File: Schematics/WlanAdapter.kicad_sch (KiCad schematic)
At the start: 28 parts, among them J1 Barrel_Jack, J2 Conn_02x05_Odd_Even, Q1 AO3400A, U3 ESP32-C3_SUPERMINI

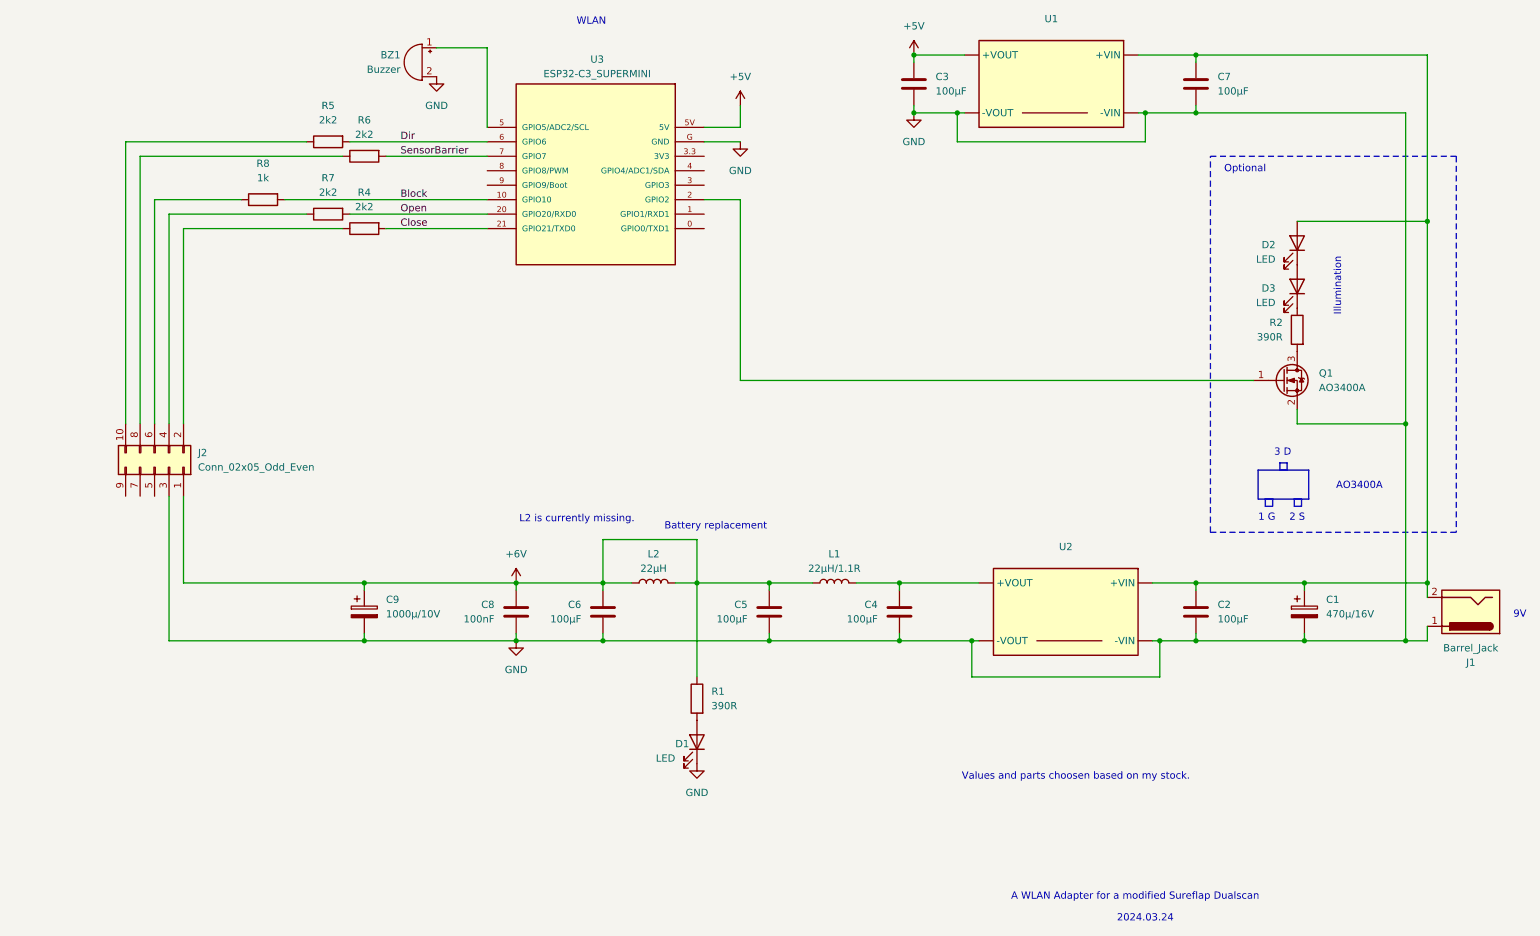
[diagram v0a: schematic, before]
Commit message: Finalize schematics, EspHome works.
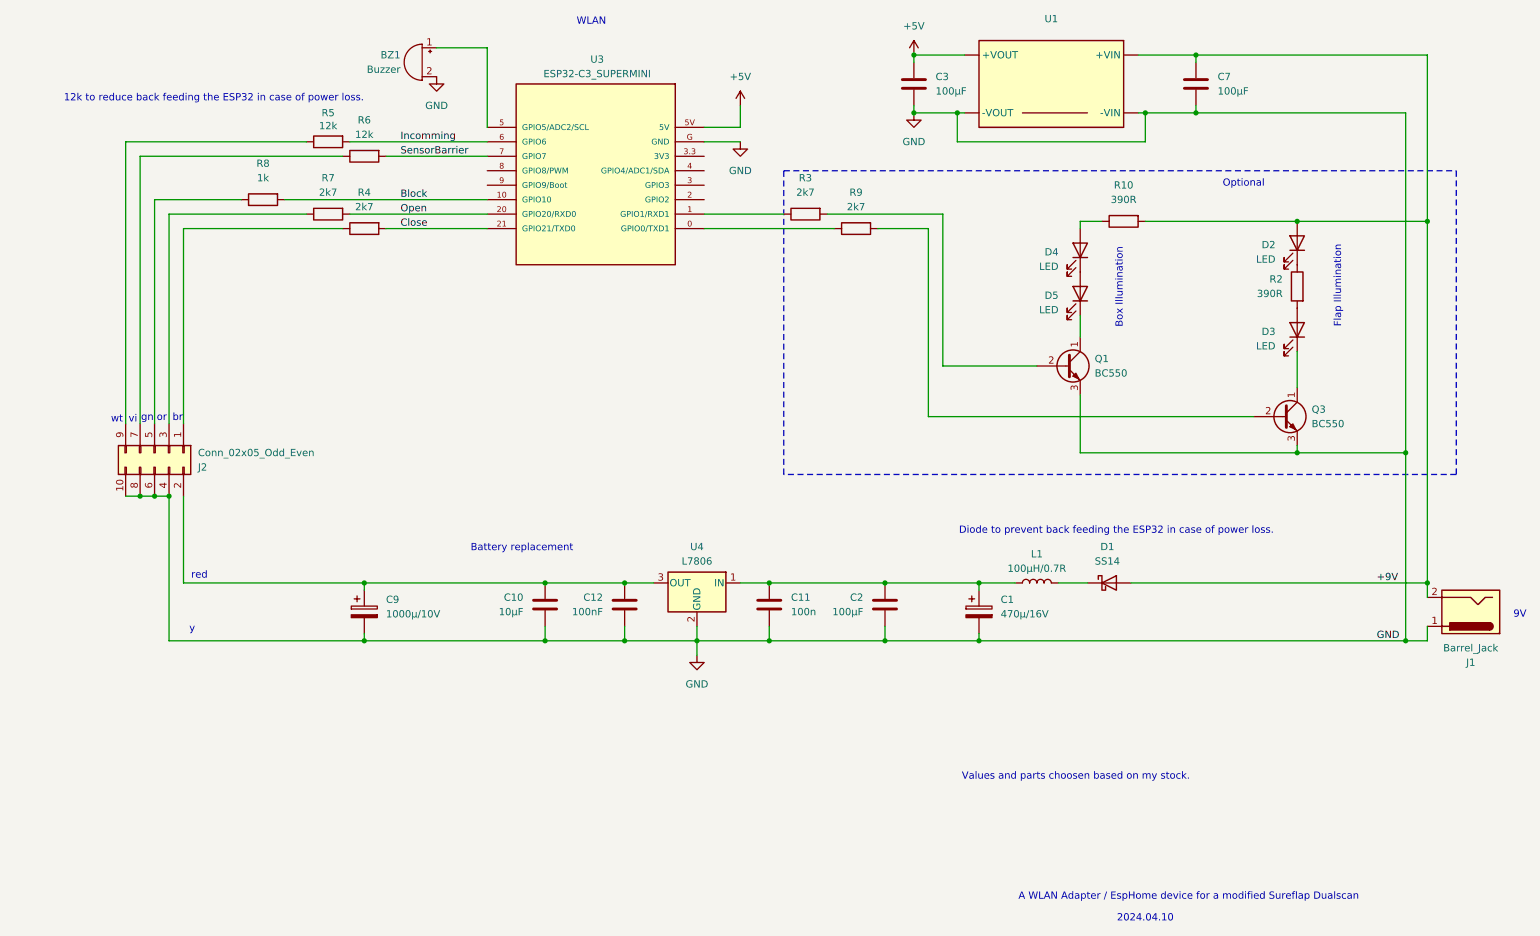
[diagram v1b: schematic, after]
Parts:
- removed C4, C5, C6: 100µF, symbol Device:C
- removed C8: 100nF, symbol Device:C
- removed D1: LED, symbol Device:LED
- removed L2: 22µH, symbol Device:L
- removed Q1: AO3400A, Package_TO_SOT_SMD:SOT-23, symbol Transistor_FET:AO3400A
- removed R1: 390R, symbol Device:R
- removed U2: ~, symbol dcdc:DCDC_VAR
- added C10: 10µF, symbol Device:C
- added C11: 100n, symbol Device:C
- added C12: 100nF, symbol Device:C
- added D1: SS14, Diode_SMD:D_SMA, symbol Diode:SS14
- added D4, D5: LED, symbol Device:LED
- added Q1, Q3: BC550, Package_TO_SOT_THT:TO-92_Inline, symbol Transistor_BJT:BC550
- added R10: 390R, symbol Device:R
- added R3, R9: 2k7, symbol Device:R
- added U4: L7806, symbol Regulator_Linear:L7806
- L1: value 22µH/1.1R -> 100µH/0.7R
- R4, R7: value 2k2 -> 2k7
- R5, R6: value 2k2 -> 12k
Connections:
- net GND: now also J2.10 (Pin_10), J2.4 (Pin_4), J2.6 (Pin_6), J2.8 (Pin_8), C10.2, C11.2, C12.2, Q1.3 (E), Q3.3 (E), U4.2 (GND); no longer J2.3 (Pin_3)
- net at R2.2: now also D3.2 (A)
- net +9V: now reaches C7.1, D2.2 (A), J1.2, U1.1 (+VIN)
- net +9V: now also D1.2 (A), R10.2; no longer C1.1, C2.1
- net at R8.1: now also J2.5 (Pin_5); no longer J2.6 (Pin_6)
- net at R4.1: now also J2.1 (Pin_1); no longer J2.2 (Pin_2)
- net at R7.1: now also J2.3 (Pin_3); no longer J2.4 (Pin_4)
- net at R2.1: now also D2.1 (K); no longer D3.1 (K)
- net at L1.1: now also D1.1 (K)
- net at U3.0 (GPIO0/TXD1): now also R9.1
- net at U3.1 (GPIO1/RXD1): now also R3.1
- net at R5.1: now also J2.9 (Pin_9); no longer J2.10 (Pin_10)
- net at R6.1: now also J2.7 (Pin_7); no longer J2.8 (Pin_8)
- removed net +6V: C9.1, J2.1 (Pin_1), L1.2
- net Dir renamed Incomming
- new net: C1.1, C11.1, C2.1, L1.2, U4.1 (IN)
- new net: C10.1, C12.1, C9.1, J2.2 (Pin_2), U4.3 (OUT)
- new net: D4.1 (K), D5.2 (A)
- new net: D4.2 (A), R10.1
- new net: D3.1 (K), Q3.1 (C)
- new net: Q1.2 (B), R3.2
- new net: D5.1 (K), Q1.1 (C)
- new net: Q3.2 (B), R9.2
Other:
- note added: "12k to reduce back feeding the ESP32 in case of power loss."
- note added: "2024.04.10"
- note added: "A WLAN Adapter / EspHome device for a modified Sureflap Dualscan"
- note added: "Box Illumination"
- note added: "Diode to prevent back feeding the ESP32 in case of power loss."
- note added: "Flap Illumination"
- note added: "br"
- note added: "gn"
- note added: "or"
- note added: "red"
- note added: "vi"
- note added: "wt"
- note added: "y"
- note removed: "1 G"
- note removed: "2 S"
- note removed: "2024.03.24"
- note removed: "3 D"
- note removed: "A WLAN Adapter for a modified Sureflap Dualscan"
- note removed: "AO3400A"
- note removed: "Illumination"
- note removed: "L2 is currently missing."
- moved on the sheet: C1, D3, R2
